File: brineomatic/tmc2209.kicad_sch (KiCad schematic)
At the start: 17 parts, among them J21 Conn_01x04, U9 TMC2209-LA

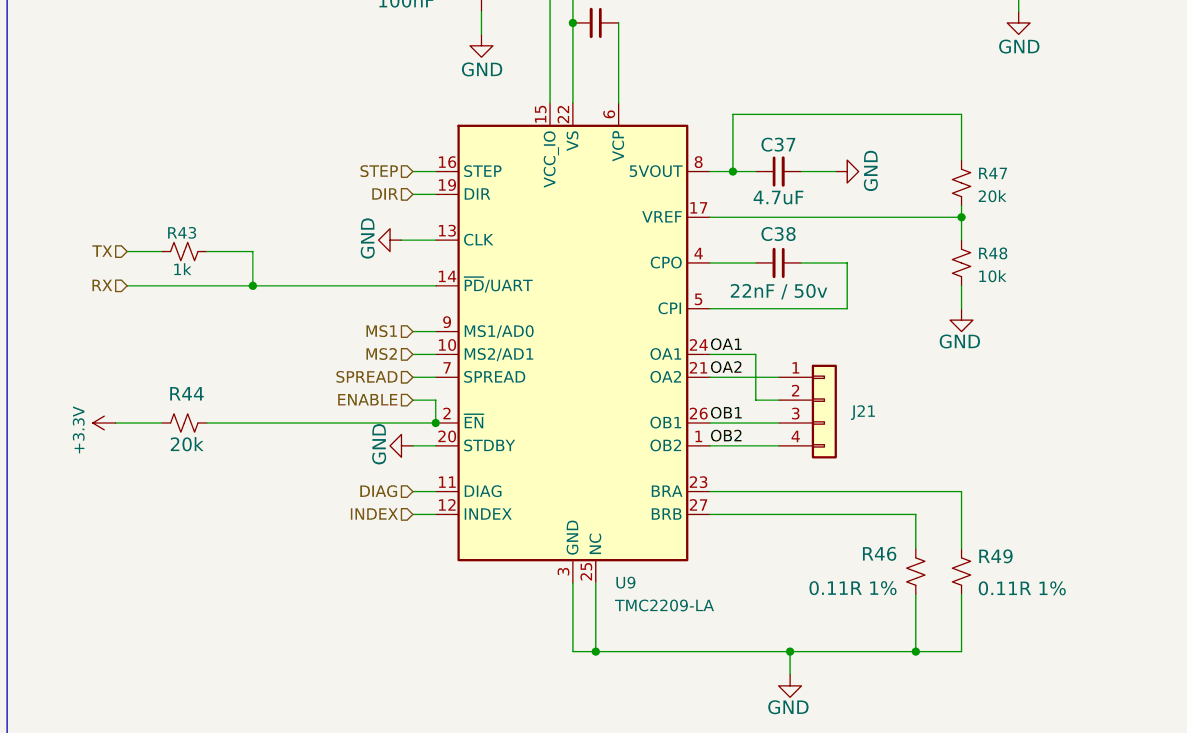
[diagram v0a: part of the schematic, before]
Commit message: put 2x0 ohm between GND and USB SHIELD
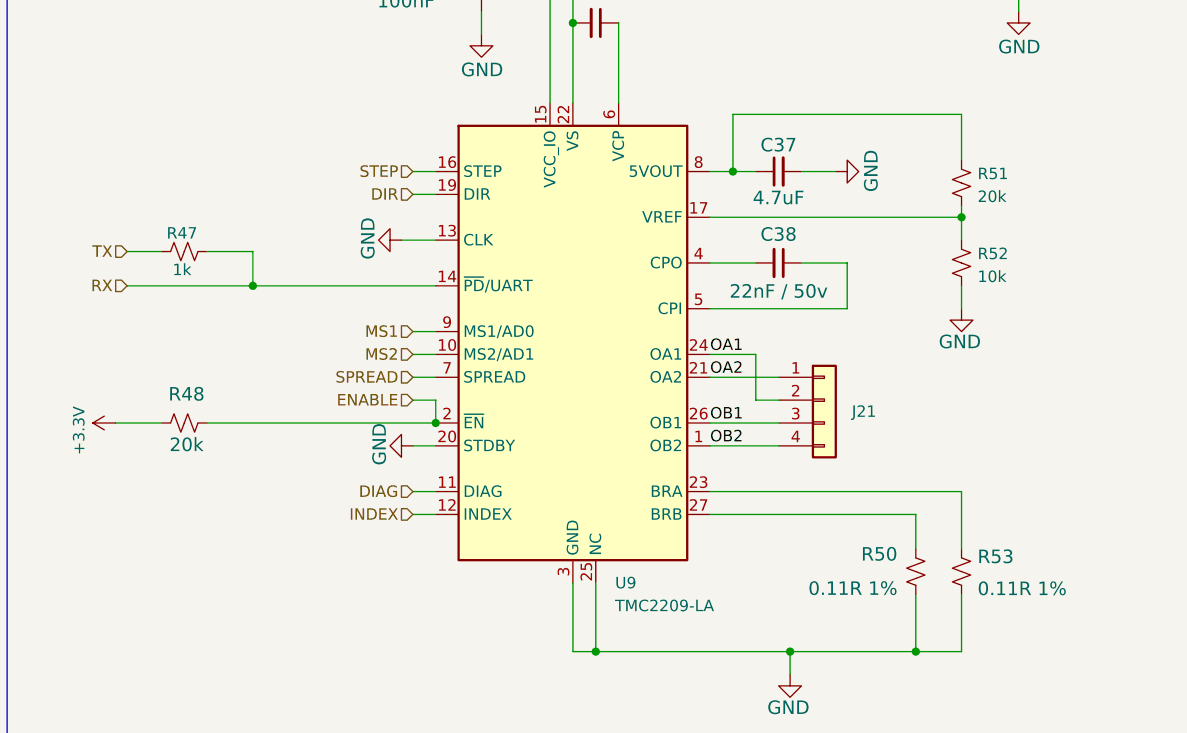
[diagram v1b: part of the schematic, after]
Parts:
- renumbered R43 to R47, R44 to R48, R46 to R50, R47 to R51, R48 to R52, R49 to R53
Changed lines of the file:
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@@
 		(on_board yes)
 		(dnp no)
-		(property "Reference" "R44"
+		(property "Reference" "R48"
 			(at 38.354 108.966 90)
 			(effects
@@
 			(project "brineomatic"
 				(path "/96477ae2-ef08-48f3-8dd4-fe4478541f68/0f01c39f-0c25-414e-9ed3-1ba09e2af0c5"
-					(reference "R44")
+					(reference "R48")
 					(unit 1)
 				)
@@
 		(on_board yes)
 		(dnp no)
-		(property "Reference" "R49"
+		(property "Reference" "R53"
 			(at 126.238 128.778 0)
 			(effects
@@
 			(project "brineomatic"
 				(path "/96477ae2-ef08-48f3-8dd4-fe4478541f68/0f01c39f-0c25-414e-9ed3-1ba09e2af0c5"
-					(reference "R49")
+					(reference "R53")
 					(unit 1)
 				)
@@
 		(on_board yes)
 		(dnp no)
-		(property "Reference" "R43"
+		(property "Reference" "R47"
 			(at 37.846 91.948 90)
 			(effects
@@
 			(project "brineomatic"
 				(path "/96477ae2-ef08-48f3-8dd4-fe4478541f68/0f01c39f-0c25-414e-9ed3-1ba09e2af0c5"
-					(reference "R43")
+					(reference "R47")
 					(unit 1)
 				)
@@
 		(on_board yes)
 		(dnp no)
-		(property "Reference" "R46"
+		(property "Reference" "R50"
 			(at 117.348 126.746 0)
 			(effects
@@
 			(project "brineomatic"
 				(path "/96477ae2-ef08-48f3-8dd4-fe4478541f68/0f01c39f-0c25-414e-9ed3-1ba09e2af0c5"
-					(reference "R46")
+					(reference "R50")
 					(unit 1)
 				)
@@
 		(on_board yes)
 		(dnp no)
-		(property "Reference" "R47"
+		(property "Reference" "R51"
 			(at 126.238 85.344 0)
 			(effects
@@
 			(project "brineomatic"
 				(path "/96477ae2-ef08-48f3-8dd4-fe4478541f68/0f01c39f-0c25-414e-9ed3-1ba09e2af0c5"
-					(reference "R47")
+					(reference "R51")
 					(unit 1)
 				)
@@
 		(on_board yes)
 		(dnp no)
-		(property "Reference" "R48"
+		(property "Reference" "R52"
 			(at 126.238 94.234 0)
 			(effects
@@
 			(project "brineomatic"
 				(path "/96477ae2-ef08-48f3-8dd4-fe4478541f68/0f01c39f-0c25-414e-9ed3-1ba09e2af0c5"
-					(reference "R48")
-					(unit 1)
-				)
+					(reference "R52")
+					(unit 1)
+				)

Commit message: add ESD and series resistor to GPIO0/EN
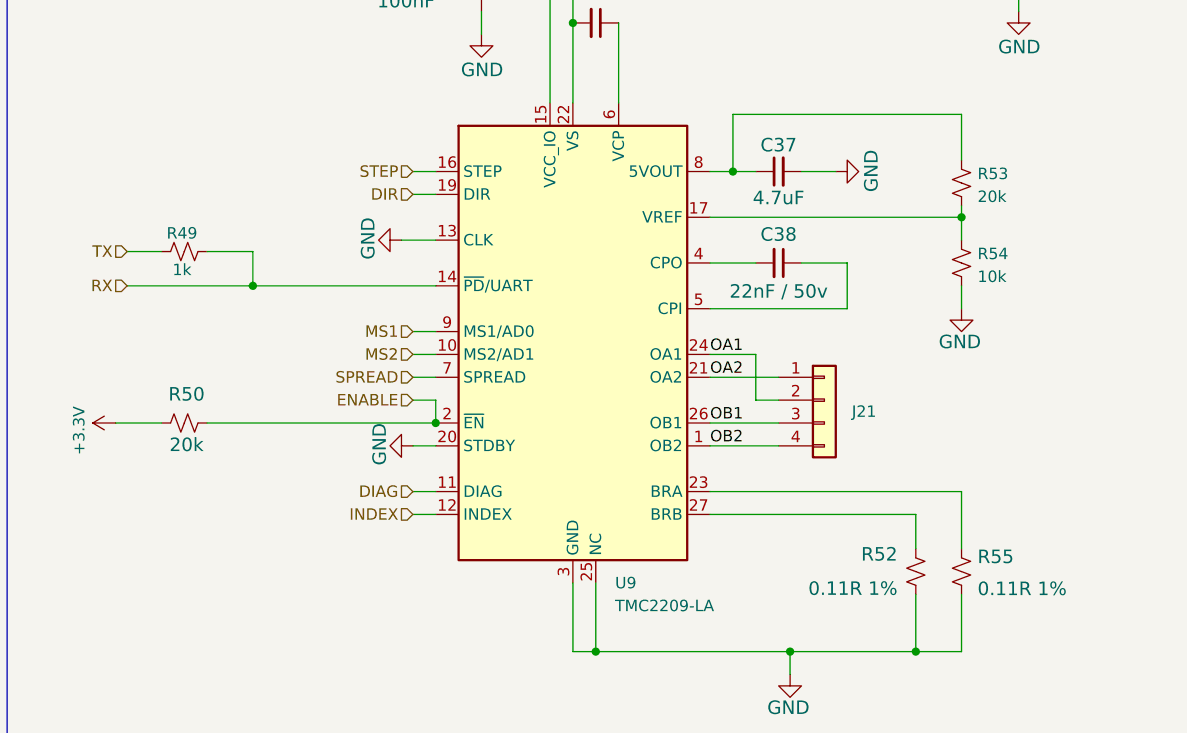
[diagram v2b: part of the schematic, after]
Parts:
- renumbered R47 to R49, R48 to R50, R50 to R52, R51 to R53, R52 to R54, R53 to R55
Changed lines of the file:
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@@
 		(on_board yes)
 		(dnp no)
-		(property "Reference" "R48"
+		(property "Reference" "R50"
 			(at 38.354 108.966 90)
 			(effects
@@
 			(project "brineomatic"
 				(path "/96477ae2-ef08-48f3-8dd4-fe4478541f68/0f01c39f-0c25-414e-9ed3-1ba09e2af0c5"
-					(reference "R48")
+					(reference "R50")
 					(unit 1)
 				)
@@
 		(on_board yes)
 		(dnp no)
-		(property "Reference" "R53"
+		(property "Reference" "R55"
 			(at 126.238 128.778 0)
 			(effects
@@
 			(project "brineomatic"
 				(path "/96477ae2-ef08-48f3-8dd4-fe4478541f68/0f01c39f-0c25-414e-9ed3-1ba09e2af0c5"
-					(reference "R53")
+					(reference "R55")
 					(unit 1)
 				)
@@
 		(on_board yes)
 		(dnp no)
-		(property "Reference" "R47"
+		(property "Reference" "R49"
 			(at 37.846 91.948 90)
 			(effects
@@
 			(project "brineomatic"
 				(path "/96477ae2-ef08-48f3-8dd4-fe4478541f68/0f01c39f-0c25-414e-9ed3-1ba09e2af0c5"
-					(reference "R47")
+					(reference "R49")
 					(unit 1)
 				)
@@
 		(on_board yes)
 		(dnp no)
-		(property "Reference" "R50"
+		(property "Reference" "R52"
 			(at 117.348 126.746 0)
 			(effects
@@
 			(project "brineomatic"
 				(path "/96477ae2-ef08-48f3-8dd4-fe4478541f68/0f01c39f-0c25-414e-9ed3-1ba09e2af0c5"
-					(reference "R50")
+					(reference "R52")
 					(unit 1)
 				)
@@
 		(on_board yes)
 		(dnp no)
-		(property "Reference" "R51"
+		(property "Reference" "R53"
 			(at 126.238 85.344 0)
 			(effects
@@
 			(project "brineomatic"
 				(path "/96477ae2-ef08-48f3-8dd4-fe4478541f68/0f01c39f-0c25-414e-9ed3-1ba09e2af0c5"
-					(reference "R51")
+					(reference "R53")
 					(unit 1)
 				)
@@
 		(on_board yes)
 		(dnp no)
-		(property "Reference" "R52"
+		(property "Reference" "R54"
 			(at 126.238 94.234 0)
 			(effects
@@
 			(project "brineomatic"
 				(path "/96477ae2-ef08-48f3-8dd4-fe4478541f68/0f01c39f-0c25-414e-9ed3-1ba09e2af0c5"
-					(reference "R52")
-					(unit 1)
-				)
+					(reference "R54")
+					(unit 1)
+				)

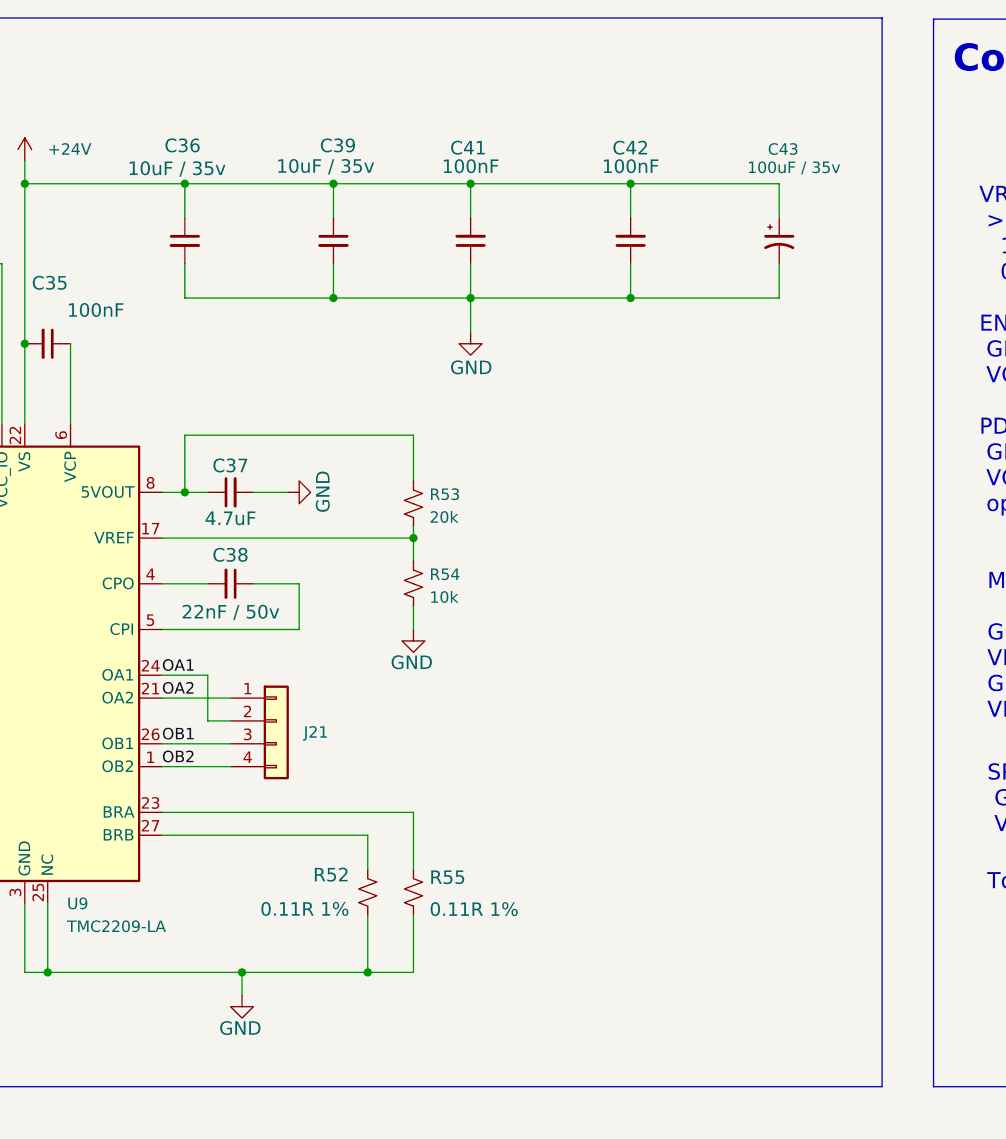
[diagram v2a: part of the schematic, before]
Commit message: tmc2209 add 470pF / 100v caps to outputs for esd protection
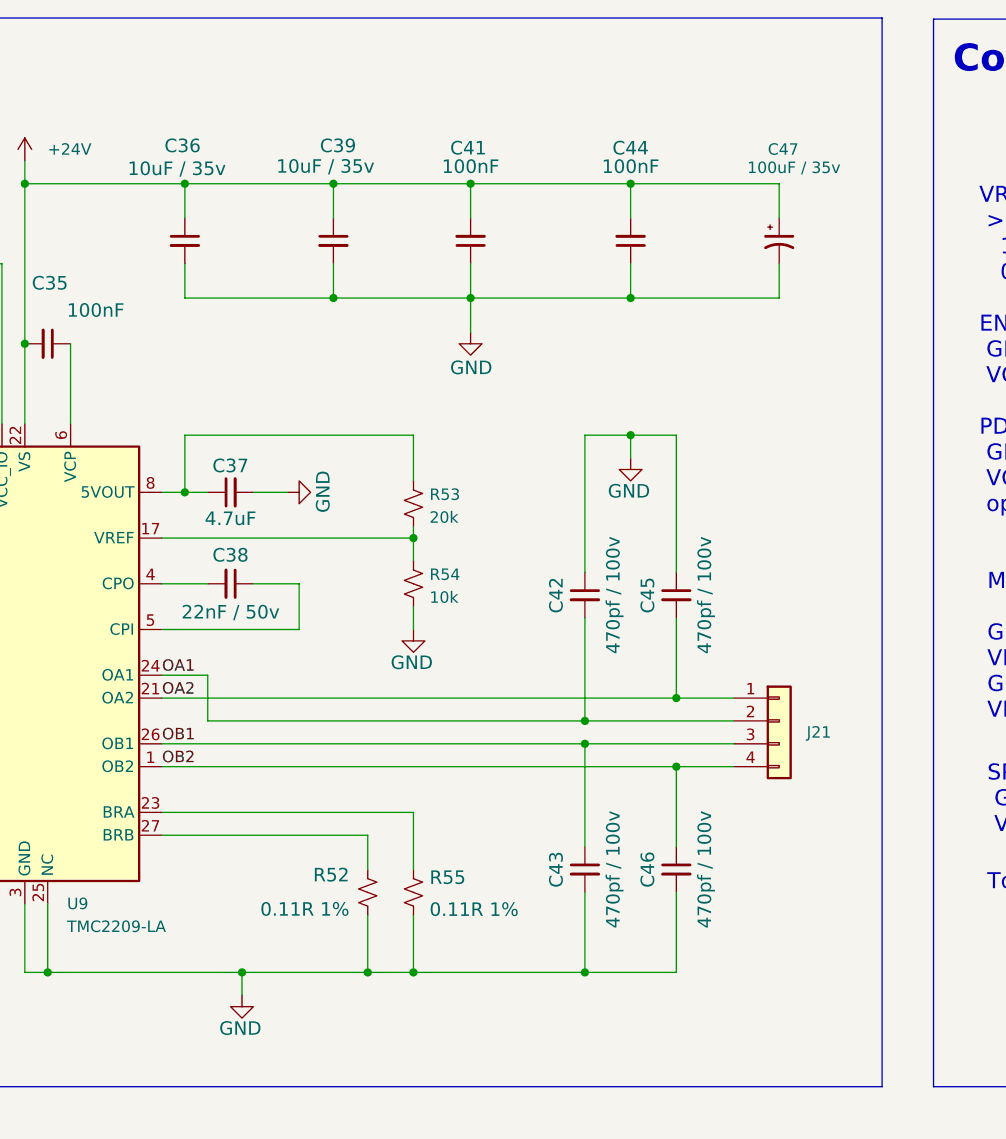
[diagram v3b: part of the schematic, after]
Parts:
- added C42, C43, C45, C46: 470pf / 100v, Capacitor_SMD:C_0603_1608Metric, symbol Device:C_Small
- renumbered C42 to C44, C43 to C47
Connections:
- net GND: now also C42.1, C43.2, C45.1, C46.2
- net OA1: now also C42.2
- net OA2: now also C45.2
- net OB1: now also C43.1
- net OB2: now also C46.1
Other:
- moved on the sheet: J21

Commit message: add inline resistor to temperature sensor + servo inputs - 100ohm
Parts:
- renumbered R49 to R52, R50 to R53, R52 to R55, R53 to R56, R54 to R57, R55 to R58
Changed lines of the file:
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@@
 		(on_board yes)
 		(dnp no)
-		(property "Reference" "R50"
+		(property "Reference" "R53"
 			(at 38.354 108.966 90)
 			(effects
@@
 			(project "brineomatic"
 				(path "/96477ae2-ef08-48f3-8dd4-fe4478541f68/0f01c39f-0c25-414e-9ed3-1ba09e2af0c5"
-					(reference "R50")
+					(reference "R53")
 					(unit 1)
 				)
@@
 		(on_board yes)
 		(dnp no)
-		(property "Reference" "R55"
+		(property "Reference" "R58"
 			(at 126.238 128.778 0)
 			(effects
@@
 			(project "brineomatic"
 				(path "/96477ae2-ef08-48f3-8dd4-fe4478541f68/0f01c39f-0c25-414e-9ed3-1ba09e2af0c5"
-					(reference "R55")
+					(reference "R58")
 					(unit 1)
 				)
@@
 		(on_board yes)
 		(dnp no)
-		(property "Reference" "R49"
+		(property "Reference" "R52"
 			(at 37.846 91.948 90)
 			(effects
@@
 			(project "brineomatic"
 				(path "/96477ae2-ef08-48f3-8dd4-fe4478541f68/0f01c39f-0c25-414e-9ed3-1ba09e2af0c5"
-					(reference "R49")
+					(reference "R52")
 					(unit 1)
 				)
@@
 		(on_board yes)
 		(dnp no)
-		(property "Reference" "R52"
+		(property "Reference" "R55"
 			(at 117.348 126.746 0)
 			(effects
@@
 			(project "brineomatic"
 				(path "/96477ae2-ef08-48f3-8dd4-fe4478541f68/0f01c39f-0c25-414e-9ed3-1ba09e2af0c5"
-					(reference "R52")
+					(reference "R55")
 					(unit 1)
 				)
@@
 		(on_board yes)
 		(dnp no)
-		(property "Reference" "R53"
+		(property "Reference" "R56"
 			(at 126.238 85.344 0)
 			(effects
@@
 			(project "brineomatic"
 				(path "/96477ae2-ef08-48f3-8dd4-fe4478541f68/0f01c39f-0c25-414e-9ed3-1ba09e2af0c5"
-					(reference "R53")
+					(reference "R56")
 					(unit 1)
 				)
@@
 		(on_board yes)
 		(dnp no)
-		(property "Reference" "R54"
+		(property "Reference" "R57"
 			(at 126.238 94.234 0)
 			(effects
@@
 			(project "brineomatic"
 				(path "/96477ae2-ef08-48f3-8dd4-fe4478541f68/0f01c39f-0c25-414e-9ed3-1ba09e2af0c5"
-					(reference "R54")
-					(unit 1)
-				)
+					(reference "R57")
+					(unit 1)
+				)

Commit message: added bulk cap after ideal diode
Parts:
- renumbered C34 to C36, C35 to C37, C36 to C38, C37 to C39, C38 to C40, C39 to C41, C41 to C43, C42 to C44, C43 to C45, C44 to C46, C45 to C47, C46 to C48, C47 to C49
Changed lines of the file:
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@@
 		(on_board yes)
 		(dnp no)
-		(property "Reference" "C39"
+		(property "Reference" "C41"
 			(at 118.11 45.72 0)
 			(effects
@@
 			(project "brineomatic"
 				(path "/96477ae2-ef08-48f3-8dd4-fe4478541f68/0f01c39f-0c25-414e-9ed3-1ba09e2af0c5"
-					(reference "C39")
+					(reference "C41")
 					(unit 1)
 				)
@@
 		(on_board yes)
 		(dnp no)
-		(property "Reference" "C44"
+		(property "Reference" "C46"
 			(at 148.59 45.974 0)
 			(effects
@@
 			(project "brineomatic"
 				(path "/96477ae2-ef08-48f3-8dd4-fe4478541f68/0f01c39f-0c25-414e-9ed3-1ba09e2af0c5"
-					(reference "C44")
+					(reference "C46")
 					(unit 1)
 				)
@@
 		(on_board yes)
 		(dnp no)
-		(property "Reference" "C35"
+		(property "Reference" "C37"
 			(at 84.074 62.738 90)
 			(effects
@@
 			(project "brineomatic"
 				(path "/96477ae2-ef08-48f3-8dd4-fe4478541f68/0f01c39f-0c25-414e-9ed3-1ba09e2af0c5"
-					(reference "C35")
+					(reference "C37")
 					(unit 1)
 				)
@@
 		(on_board yes)
 		(dnp no)
-		(property "Reference" "C45"
+		(property "Reference" "C47"
 			(at 151.384 96.52 90)
 			(effects
@@
 			(project "brineomatic"
 				(path "/96477ae2-ef08-48f3-8dd4-fe4478541f68/0f01c39f-0c25-414e-9ed3-1ba09e2af0c5"
-					(reference "C45")
+					(reference "C47")
 					(unit 1)
 				)
@@
 		(on_board yes)
 		(dnp no)
-		(property "Reference" "C43"
+		(property "Reference" "C45"
 			(at 141.224 127 90)
 			(effects
@@
 			(project "brineomatic"
 				(path "/96477ae2-ef08-48f3-8dd4-fe4478541f68/0f01c39f-0c25-414e-9ed3-1ba09e2af0c5"
-					(reference "C43")
+					(reference "C45")
 					(unit 1)
 				)
@@
 		(on_board yes)
 		(dnp no)
-		(property "Reference" "C47"
+		(property "Reference" "C49"
 			(at 163.83 46.99 0)
 			(effects
@@
 			(project ""
 				(path "/96477ae2-ef08-48f3-8dd4-fe4478541f68/0f01c39f-0c25-414e-9ed3-1ba09e2af0c5"
-					(reference "C47")
+					(reference "C49")
 					(unit 1)
 				)
@@
 		(on_board yes)
 		(dnp no)
-		(property "Reference" "C36"
+		(property "Reference" "C38"
 			(at 100.838 45.72 0)
 			(effects
@@
 			(project "brineomatic"
 				(path "/96477ae2-ef08-48f3-8dd4-fe4478541f68/0f01c39f-0c25-414e-9ed3-1ba09e2af0c5"
-					(reference "C36")
+					(reference "C38")
 					(unit 1)
 				)
@@
 		(on_board yes)
 		(dnp no)
-		(property "Reference" "#PWR063"
+		(property "Reference" "#PWR065"
 			(at 74.93 63.5 0)
 			(effects
@@
 			(project "brineomatic"
 				(path "/96477ae2-ef08-48f3-8dd4-fe4478541f68/0f01c39f-0c25-414e-9ed3-1ba09e2af0c5"
-					(reference "#PWR063")
+					(reference "#PWR065")
 					(unit 1)
 				)
@@
 		(on_board yes)
 		(dnp no)
-		(property "Reference" "#PWR062"
+		(property "Reference" "#PWR064"
 			(at 34.29 113.03 0)
 			(effects
@@
 			(project "brineomatic"
 				(path "/96477ae2-ef08-48f3-8dd4-fe4478541f68/0f01c39f-0c25-414e-9ed3-1ba09e2af0c5"
-					(reference "#PWR062")
+					(reference "#PWR064")
 					(unit 1)
 				)
@@
 		(on_board yes)
 		(dnp no)
-		(property "Reference" "C42"
+		(property "Reference" "C44"
 			(at 141.224 96.52 90)
 			(effects
@@
 			(project "brineomatic"
 				(path "/96477ae2-ef08-48f3-8dd4-fe4478541f68/0f01c39f-0c25-414e-9ed3-1ba09e2af0c5"
-					(reference "C42")
+					(reference "C44")
 					(unit 1)
 				)
@@
 		(on_board yes)
 		(dnp no)
-		(property "Reference" "C46"
+		(property "Reference" "C48"
 			(at 151.384 127 90)
 			(effects
@@
 			(project "brineomatic"
 				(path "/96477ae2-ef08-48f3-8dd4-fe4478541f68/0f01c39f-0c25-414e-9ed3-1ba09e2af0c5"
-					(reference "C46")
+					(reference "C48")
 					(unit 1)
 				)
@@
 		(on_board yes)
 		(dnp no)
-		(property "Reference" "C34"
+		(property "Reference" "C36"
 			(at 66.04 63.754 0)
 			(effects
@@
 			(project "brineomatic"
 				(path "/96477ae2-ef08-48f3-8dd4-fe4478541f68/0f01c39f-0c25-414e-9ed3-1ba09e2af0c5"
-					(reference "C34")
+					(reference "C36")
 					(unit 1)
 				)
@@
 		(dnp no)
 		(fields_autoplaced yes)
-		(property "Reference" "#PWR064"
+		(property "Reference" "#PWR066"
 			(at 81.28 52.07 0)
 			(effects
@@
 			(project ""
 				(path "/96477ae2-ef08-48f3-8dd4-fe4478541f68/0f01c39f-0c25-414e-9ed3-1ba09e2af0c5"
-					(reference "#PWR064")
+					(reference "#PWR066")
 					(unit 1)
 				)
@@
 		(on_board yes)
 		(dnp no)
-		(property "Reference" "C38"
+		(property "Reference" "C40"
 			(at 104.14 92.964 90)
 			(effects
@@
 			(project "brineomatic"
 				(path "/96477ae2-ef08-48f3-8dd4-fe4478541f68/0f01c39f-0c25-414e-9ed3-1ba09e2af0c5"
-					(reference "C38")
+					(reference "C40")
 					(unit 1)
 				)
@@
 		(on_board yes)
 		(dnp no)
-		(property "Reference" "C37"
+		(property "Reference" "C39"
 			(at 104.14 81.28 90)
 			(effects
@@
 			(project "brineomatic"
 				(path "/96477ae2-ef08-48f3-8dd4-fe4478541f68/0f01c39f-0c25-414e-9ed3-1ba09e2af0c5"
-					(reference "C37")
+					(reference "C39")
 					(unit 1)
 				)
@@
 		(on_board yes)
 		(dnp no)
-		(property "Reference" "C41"
+		(property "Reference" "C43"
 			(at 130.556 45.974 0)
 			(effects
@@
 			(project "brineomatic"
 				(path "/96477ae2-ef08-48f3-8dd4-fe4478541f68/0f01c39f-0c25-414e-9ed3-1ba09e2af0c5"
-					(reference "C41")
-					(unit 1)
-				)
+					(reference "C43")
+					(unit 1)
+				)
